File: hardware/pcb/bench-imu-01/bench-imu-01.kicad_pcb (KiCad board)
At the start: 4 copper layers, 150 x 95 mm, 52 parts, among them J1 USB_C_Receptacle_GCT_USB4105-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, J2 PinHeader_1x04_P2.54mm_Vertic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, J3 PinHeader_1x04_P2.54mm_Vertic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, J4 BarrelJack_CUI_PJ-102AH_Horiz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, M1 TerminalBlock_MaiXu_MX126-5.0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, SW1 SW_PUSH_6mm, U1 LQFP-32_7x7mm_P0.8mm, U2 Bosch_LGA-14_3x2.5mm_P0.5mm, U3 SOT-23-5, U4 SOT-23-6, U5 HTSSOP-24-1EP_4.4x7.8mm_P0.65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, U6 HTSSOP-20-1EP_4.4x6.5mm_P0.65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

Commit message: PCB Engineer: fix ISS-030 (CRITICAL), ISS-033/034/035 (HIGH/MEDIUM), partial ISS-031 (HIGH)
Post-Hardware-Reviewer-Cycle-6 fix round. Fixes real bugs the independent
review found in the Rev 3-5 motor-subsystem schematic transcription and
first PCB layout (validation/design-review.md, commit 84db343).

ISS-030 (CRITICAL, RESOLVED): U1 pin 19 (PA9) was never actually a member
of the /U6_EN net despite a wire being drawn to it -- the shared
MCU_ST_STM32G0 library symbol declares pin 19's base electrical type as
no_connect, with PA9 only reachable via KiCad's per-instance "alternate
pin function" mechanism, which kiutils 1.4.8 cannot express. Fixed with a
patch_alternate_pin_function() post-processing step in
generate_schematic.py that injects (alternate "PA9") inside the
(pin "19" ...) s-expression directly in the raw .kicad_sch text (inserting
it as a sibling line instead breaks the file -- caught via kicad-cli sch
erc failing to parse during development of the fix). Verified via ERC
(0 errors, only the 1 pre-existing benign U3 lib_symbol_mismatch warning
remains) and kicad-cli sch export netlist (U1 pin 19 now confirmed a
genuine member of /U6_EN).

ISS-033/034/035 (HIGH/HIGH/MEDIUM, RESOLVED): generate_pcb.py's net
assignment used fp.FindPadByNumber(pin), which returns only the FIRST
physical pad when a footprint legitimately has several sharing one pad
number (U6's 17-sub-pad PowerPAD, J1's 4-pad USB shield, SW1's doubled
terminal pads) -- leaving every other same-numbered physical pad
genuinely unnetted, invisible to DRC's unconnected_items check. Fixed by
enumerating every matching physical pad and locally bridging them (a
same-number pad-to-pad track, independent of the later MST/Step-A routing
which only operates at (ref, pin) granularity). Independently
re-verified via a standalone pad/net audit script (not just re-trusting
the same DRC proxy that missed the bug originally): all of U6's 17
sub-pads, J1's 4 shield pads, and SW1's duplicate pads now share their
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
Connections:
- U1 pad 19: (no net) -> U6_EN
- U5 pad 25: (no net) -> GND
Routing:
- net GND: track 552.4 -> 635.8 mm
- net U6_EN: track 38.3 -> 87.5 mm
- net NRST: track 37.0 -> 43.5 mm

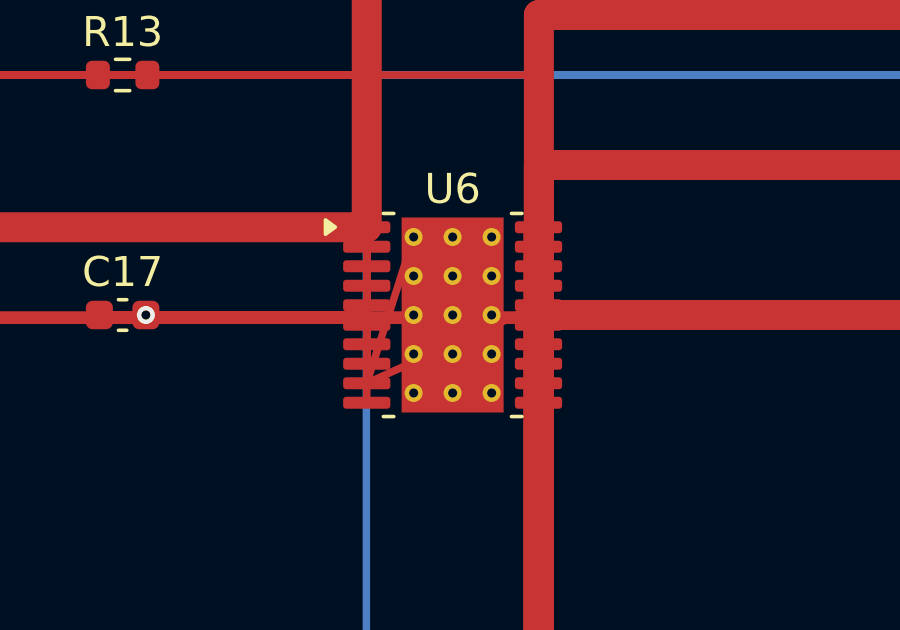
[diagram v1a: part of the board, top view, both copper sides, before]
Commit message: PCB Engineer: fix ISS-038 (HIGH) -- redundant PowerPAD bridge tracks crossing U6_ILIM
Same-day follow-up after Hardware Reviewer Cycle 7 (commit 89a158c)
independently confirmed the ISS-030/033/034/035 fix round but caught a
real new defect in it: the ISS-033/034/035 multi-pad bridging step added
16 bridge tracks under U6's PowerPAD, all of them electrically redundant
(every pad in the "21" group already shares copper via the large F.Cu/
B.Cu exposed-pad land), yet 12 of them crossed the unrelated U6_ILIM net
running through that same dense region -- trading 7 pre-existing
shorting_items for 12 new tracks_crossing violations.

Root cause: the bridging logic picked matching_pads[0] (an arbitrary
small 0.6x0.6mm thermal-via pad, footprint-file order) as its hub/
reference point and pairwise bounding-box-tested every OTHER pad in the
group against that one arbitrary via. Neighbouring 0.6mm vias spaced
1.3mm apart never geometrically intersect each other directly, so every
one was (wrongly) judged to need its own bridge -- even though all 15
vias, plus the two large land pads, are members of the very same
pad-number group, and every via's bounding box sits INSIDE the land
pads' much larger bounding boxes.

Fixed by selecting the hub pad as the largest-bounding-box-area member
of the group (`max(matching_pads, key=lambda p: p.GetBoundingBox().GetArea())`)
instead of index 0. This correctly identifies the shared copper land as
the hub for U6's PowerPAD group (0 bridges now needed, was 16) while
leaving J1's shield (3 bridges) and SW1's terminal pads (1 bridge each)
-- which have no single large land pad -- correctly still bridged.

Verified: an independent bounding-box audit confirms U6 pad-21 needs 0
bridges (was 16). kicad-cli pcb drc --format json, net-pair-parsed,
confirms GND-vs-U6_ILIM crossings dropped 12 -> 1 across a fresh 4-run
DRC re-check (the remaining 1 matches Cycle 6's own documented
pre-existing, unrelated crossing in that same region). The standalone
pad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
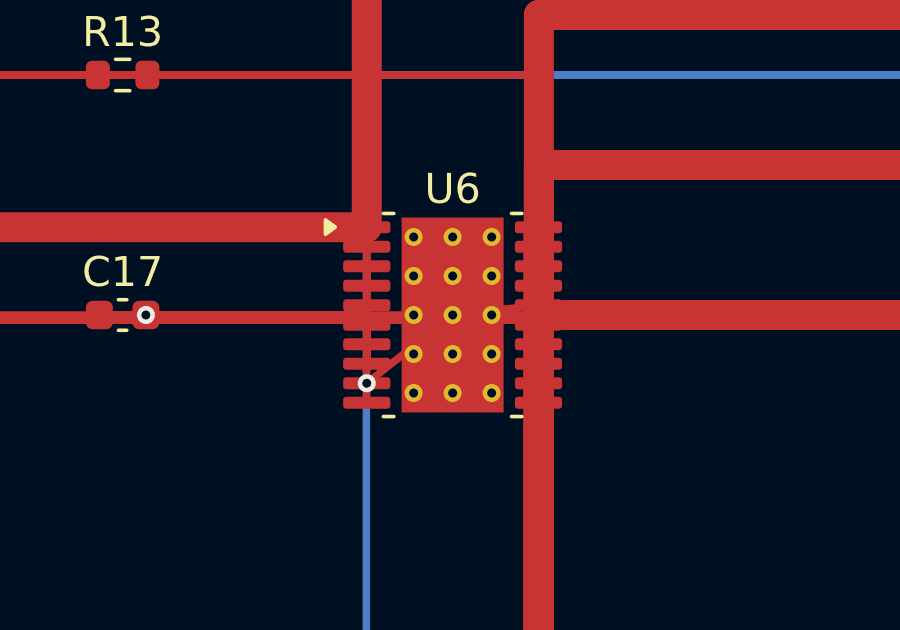
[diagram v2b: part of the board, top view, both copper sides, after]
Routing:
- net GND: track 635.8 -> 574.1 mm, vias 28 -> 29
